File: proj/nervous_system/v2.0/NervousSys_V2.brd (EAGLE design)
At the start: 162.3 x 94.7 mm, 101 parts, among them IC2 PCA9615DP, IC3 PCA9615DP, IC4 PCA9615DP, IC5 PCA9615DP, IC6 PCA9615DP, IC7 PCA9615DP, IC8 PCA9615DP, IC9 PCA9615DP, J2 54602-908LF, J3 54602-908LF, J4 54602-908LF, J5 54602-908LF, J6 54602-908LF, J7 54602-908LF, J8 54602-908LF, J9 54602-908LF, T1 R-78E5.0-1.0, U1 TCA9548APWRPW24-M

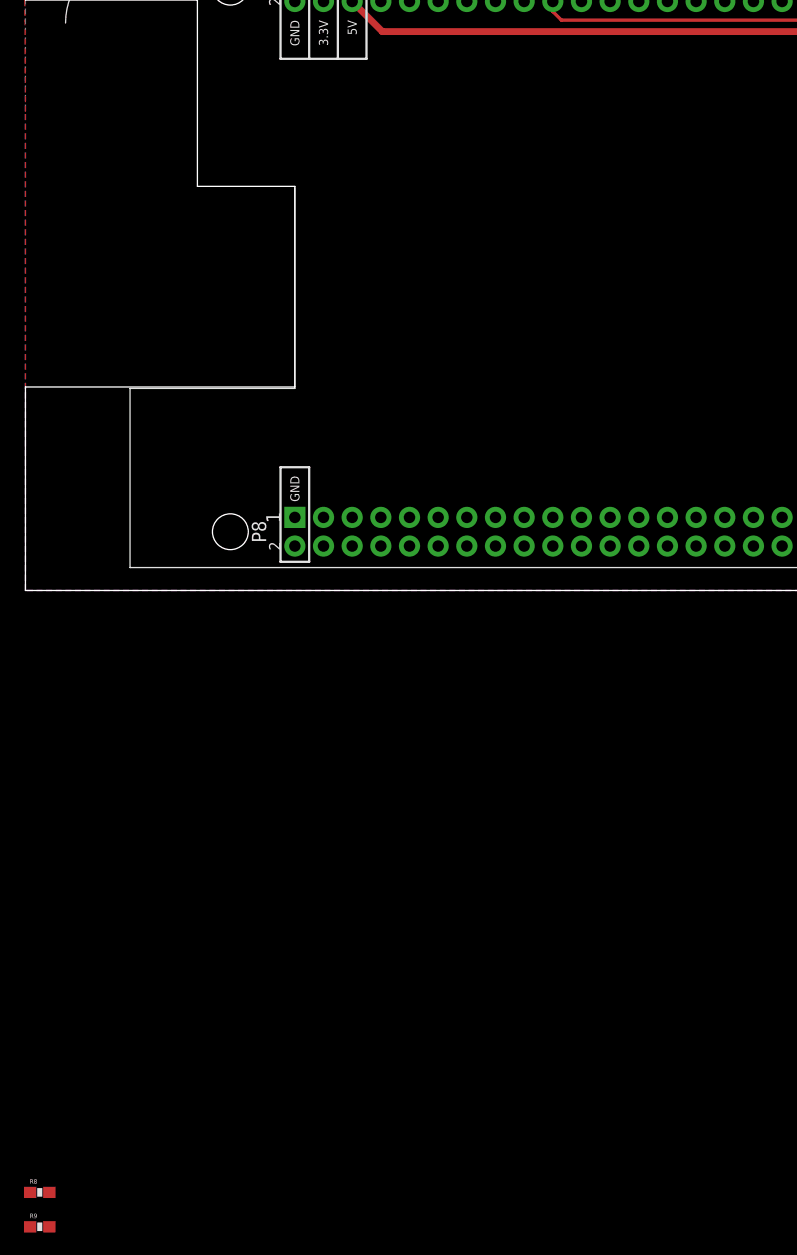
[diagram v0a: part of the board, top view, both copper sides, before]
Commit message: NS V2 Layout Change
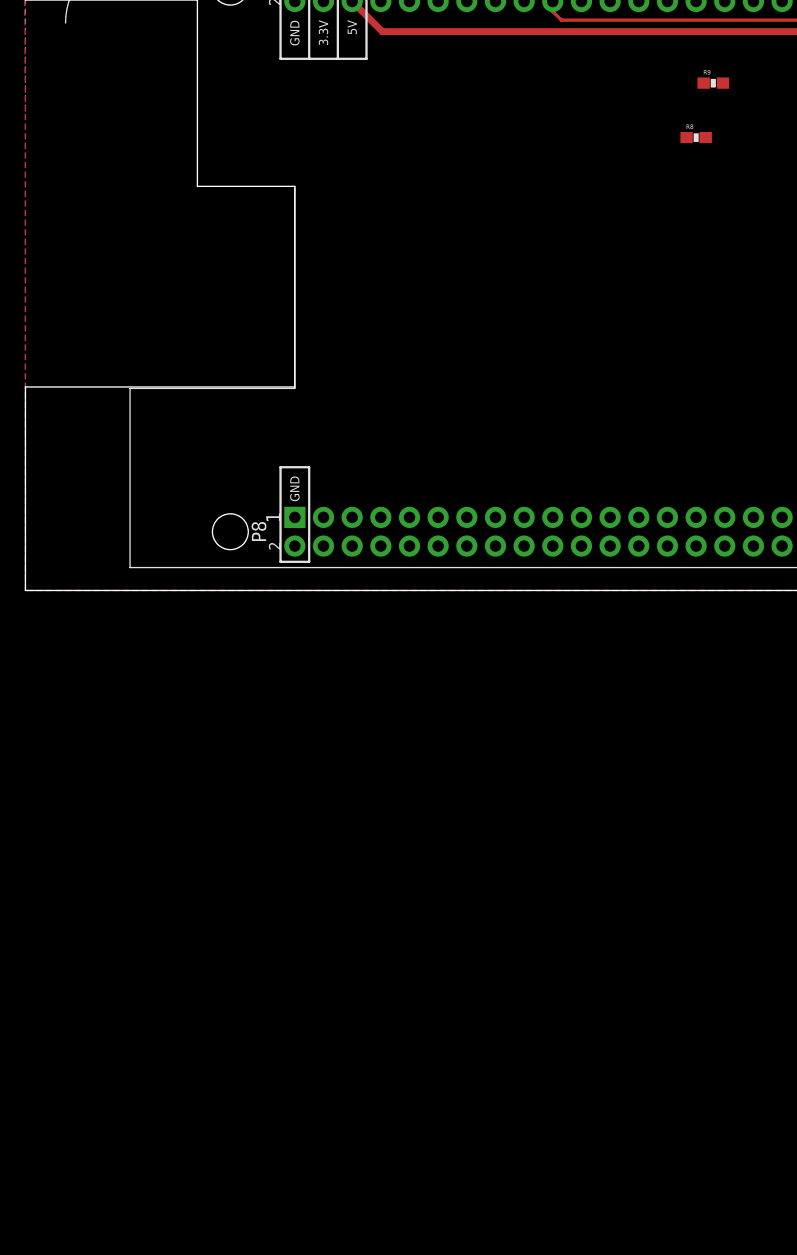
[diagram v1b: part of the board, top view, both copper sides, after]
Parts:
- moved R9 117.6 mm to (61.0, 45.0)
- moved R8 110.1 mm to (59.4, 40.1)
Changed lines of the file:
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@@
 </element>
 <element name="U$1" library="PJ-036ah" package="PJ-036AH" value="PJ-036AH" x="128.27" y="11.176" rot="R90"/>
-<element name="R8" library="SparkFun-Resistors" package="0603-RES" value="10K" x="1.27" y="-53.34">
-<attribute name="PROD_ID" value="RES-00824" x="1.27" y="-53.34" size="1.778" layer="27" display="off"/>
+<element name="R8" library="SparkFun-Resistors" package="0603-RES" value="10K" x="59.436" y="40.132">
+<attribute name="PROD_ID" value="RES-00824" x="59.436" y="40.132" size="1.778" layer="27" display="off"/>
 </element>
-<element name="R9" library="SparkFun-Resistors" package="0603-RES" value="10K" x="1.27" y="-56.388">
-<attribute name="PROD_ID" value="RES-00824" x="1.27" y="-56.388" size="1.778" layer="27" display="off"/>
+<element name="R9" library="SparkFun-Resistors" package="0603-RES" value="10K" x="60.96" y="44.958">
+<attribute name="PROD_ID" value="RES-00824" x="60.96" y="44.958" size="1.778" layer="27" display="off"/>
 </element>
 </elements>
@@
 <wire x1="82.55" y1="47.244" x2="79.248" y2="50.546" width="0.3048" layer="1"/>
 <contactref element="R9" pad="1"/>
-<wire x1="0.42" y1="-56.388" x2="47.498" y2="50.546" width="0" layer="19" extent="1-1"/>
+<wire x1="60.11" y1="44.958" x2="47.498" y2="50.546" width="0" layer="19" extent="1-1"/>
 </signal>
 <signal name="SCL">
@@
 <wire x1="57.91946875" y1="59.944" x2="47.752" y2="59.944" width="0.3048" layer="1"/>
 <contactref element="R8" pad="1"/>
-<wire x1="0.42" y1="-53.34" x2="46.736" y2="54.737" width="0" layer="19" extent="1-1"/>
+<wire x1="58.586" y1="40.132" x2="46.736" y2="54.737" width="0" layer="19" extent="1-1"/>
 </signal>
 <signal name="+3V3">
@@
 <contactref element="R9" pad="2"/>
 <wire x1="26.416" y1="54.737" x2="26.416" y2="52.197" width="0" layer="19" extent="1-1"/>
-<wire x1="2.12" y1="-53.34" x2="26.416" y2="52.197" width="0" layer="19" extent="1-1"/>
-<wire x1="2.12" y1="-56.388" x2="2.12" y2="-53.34" width="0" layer="19" extent="1-1"/>
+<wire x1="60.286" y1="40.132" x2="26.416" y2="52.197" width="0" layer="19" extent="1-1"/>
+<wire x1="61.81" y1="44.958" x2="60.286" y2="40.132" width="0" layer="19" extent="1-1"/>
 </signal>
 <signal name="RESET1">

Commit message: NSV2 Changes
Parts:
- moved R8 23.6 mm to (43.9, 57.9), turned to 180 degrees
- moved R9 16.9 mm to (44.2, 47.2), turned to 180 degrees
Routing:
- net +3V3: track 345.1 -> 383.7 mm
- net SDA: track 122.7 -> 132.7 mm, vias 0 -> 2
- net SCL: track 116.8 -> 118.7 mm
- net +5V: track 142.9 -> 144.4 mm
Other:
- board text added: "SCL Pullup"
- board text added: "SDA Pullup"
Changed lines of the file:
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@@
 <text x="7.112" y="56.896" size="1.778" layer="25">I2C
 CH:7</text>
+<text x="36.322" y="58.674" size="0.8128" layer="25">SCL Pullup</text>
+<text x="41.656" y="44.958" size="0.8128" layer="25">SDA Pullup</text>
 </plain>
 <attributes>
@@
 </element>
 <element name="U$1" library="PJ-036ah" package="PJ-036AH" value="PJ-036AH" x="128.27" y="11.176" rot="R90"/>
-<element name="R8" library="SparkFun-Resistors" package="0603-RES" value="10K" x="59.436" y="40.132">
-<attribute name="PROD_ID" value="RES-00824" x="59.436" y="40.132" size="1.778" layer="27" display="off"/>
-</element>
-<element name="R9" library="SparkFun-Resistors" package="0603-RES" value="10K" x="60.96" y="44.958">
-<attribute name="PROD_ID" value="RES-00824" x="60.96" y="44.958" size="1.778" layer="27" display="off"/>
+<element name="R8" library="SparkFun-Resistors" package="0603-RES" value="10K" x="43.942" y="57.912" rot="R180">
+<attribute name="PROD_ID" value="RES-00824" x="43.942" y="57.912" size="1.778" layer="27" rot="R180" display="off"/>
+</element>
+<element name="R9" library="SparkFun-Resistors" package="0603-RES" value="10K" x="44.196" y="47.244" rot="R180">
+<attribute name="PROD_ID" value="RES-00824" x="44.196" y="47.244" size="1.778" layer="27" rot="R180" display="off"/>
 </element>
 </elements>
@@
 <vertex x="154.686" y="73.66"/>
 <vertex x="1.016" y="73.66"/>
-<vertex x="1.016" y="94.742"/>
-<vertex x="161.798" y="94.742"/>
+<vertex x="1.524" y="95.25"/>
+<vertex x="162.306" y="95.25"/>
 <vertex x="161.798" y="33.528"/>
 </polygon>
@@
 <wire x1="87.376" y1="48.768" x2="85.852" y2="47.244" width="0.3048" layer="1"/>
 <wire x1="85.852" y1="47.244" x2="82.55" y2="47.244" width="0.3048" layer="1"/>
-<wire x1="79.248" y1="50.546" x2="47.498" y2="50.546" width="0.3048" layer="1"/>
+<wire x1="79.248" y1="50.546" x2="49.53" y2="50.546" width="0.3048" layer="1"/>
+<wire x1="49.53" y1="50.546" x2="47.498" y2="50.546" width="0.3048" layer="1"/>
 <wire x1="47.498" y1="50.546" x2="46.736" y2="51.308" width="0.3048" layer="1"/>
 <wire x1="46.736" y1="51.308" x2="46.736" y2="52.197" width="0.3048" layer="1"/>
 <wire x1="82.55" y1="47.244" x2="79.248" y2="50.546" width="0.3048" layer="1"/>
 <contactref element="R9" pad="1"/>
-<wire x1="60.11" y1="44.958" x2="47.498" y2="50.546" width="0" layer="19" extent="1-1"/>
+<wire x1="45.046" y1="47.244" x2="46.57" y2="45.72" width="0.3048" layer="1"/>
+<wire x1="46.57" y1="45.72" x2="49.53" y2="45.72" width="0.3048" layer="1"/>
+<via x="49.53" y="45.72" extent="1-16" drill="0.35"/>
+<wire x1="49.53" y1="45.72" x2="49.53" y2="49.276" width="0.3048" layer="16"/>
+<via x="49.53" y="49.276" extent="1-16" drill="0.35"/>
+<wire x1="49.53" y1="49.276" x2="49.53" y2="50.546" width="0.3048" layer="1"/>
 </signal>
 <signal name="SCL">
@@
 <wire x1="77.0479125" y1="58.90334375" x2="58.960125" y2="58.90334375" width="0.3048" layer="1"/>
 <wire x1="47.752" y1="59.944" x2="46.736" y2="58.928" width="0.3048" layer="1"/>
-<wire x1="46.736" y1="58.928" x2="46.736" y2="54.737" width="0.3048" layer="1"/>
+<wire x1="46.736" y1="58.928" x2="46.736" y2="57.912" width="0.3048" layer="1"/>
+<wire x1="46.736" y1="57.912" x2="46.736" y2="54.737" width="0.3048" layer="1"/>
 <wire x1="57.91946875" y1="59.944" x2="47.752" y2="59.944" width="0.3048" layer="1"/>
 <contactref element="R8" pad="1"/>
-<wire x1="58.586" y1="40.132" x2="46.736" y2="54.737" width="0" layer="19" extent="1-1"/>
+<wire x1="44.792" y1="57.912" x2="46.736" y2="57.912" width="0.3048" layer="1"/>
 </signal>
 <signal name="+3V3">
@@
 <contactref element="R8" pad="2"/>
 <contactref element="R9" pad="2"/>
+<wire x1="43.346" y1="47.244" x2="42.076" y2="48.514" width="0.3048" layer="1"/>
+<wire x1="42.076" y1="48.514" x2="27.686" y2="48.514" width="0.3048" layer="1"/>
+<wire x1="27.686" y1="48.514" x2="26.162" y2="50.038" width="0.3048" layer="1"/>
+<wire x1="26.162" y1="50.038" x2="26.162" y2="51.943" width="0.3048" layer="1"/>
+<wire x1="26.162" y1="51.943" x2="26.416" y2="52.197" width="0.3048" layer="1"/>
+<wire x1="43.092" y1="57.912" x2="29.591" y2="57.912" width="0.3048" layer="1"/>
+<wire x1="29.591" y1="57.912" x2="26.416" y2="54.737" width="0.3048" layer="1"/>
 <wire x1="26.416" y1="54.737" x2="26.416" y2="52.197" width="0" layer="19" extent="1-1"/>
-<wire x1="60.286" y1="40.132" x2="26.416" y2="52.197" width="0" layer="19" extent="1-1"/>
-<wire x1="61.81" y1="44.958" x2="60.286" y2="40.132" width="0" layer="19" extent="1-1"/>
 </signal>
 <signal name="RESET1">
@@
 <wire x1="86.16763125" y1="46.482" x2="88.138" y2="48.45236875" width="0.6096" layer="1"/>
 <wire x1="88.138" y1="48.45236875" x2="88.138" y2="55.31036875" width="0.6096" layer="1"/>
-<wire x1="31.623" y1="49.53" x2="79.18636875" y2="49.53" width="0.6096" layer="1"/>
+<wire x1="31.623" y1="49.53" x2="46.736" y2="49.53" width="0.6096" layer="1"/>
+<wire x1="46.736" y1="49.53" x2="48.514" y2="47.752" width="0.6096" layer="1"/>
+<wire x1="48.514" y1="47.752" x2="51.054" y2="47.752" width="0.6096" layer="1"/>
+<wire x1="51.054" y1="47.752" x2="52.832" y2="49.53" width="0.6096" layer="1"/>
+<wire x1="52.832" y1="49.53" x2="79.18636875" y2="49.53" width="0.6096" layer="1"/>
 <wire x1="88.930815625" y1="56.103184375" x2="96.096228125" y2="56.103184375" width="0.6096" layer="1"/>
 <wire x1="120.5484" y1="53.7972" x2="122.7836" y2="51.562" width="0.6096" layer="1"/>

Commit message: NSV2
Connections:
- net +3V3: no longer IC2.10, IC3.10, IC4.10, IC5.10, IC6.10, IC7.10, IC8.10, IC9.10, R18.1, R19.2, R26.1, R27.2, R34.1, R35.2, R42.1, R43.2, R50.1, R51.2, R58.1, R59.2, R66.1, R67.2, R74.1, R75.2
- net +5V: now also IC2.10, IC3.10, IC4.10, IC5.10, IC6.10, IC7.10, IC8.10, IC9.10, R18.1, R19.2, R26.1, R27.2, R34.1, R35.2, R42.1, R43.2, R50.1, R51.2, R58.1, R59.2, R66.1, R67.2, R74.1, R75.2
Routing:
- net +5V: track 144.4 -> 363.8 mm, vias 0 -> 9
- net +3V3: track 383.7 -> 304.4 mm

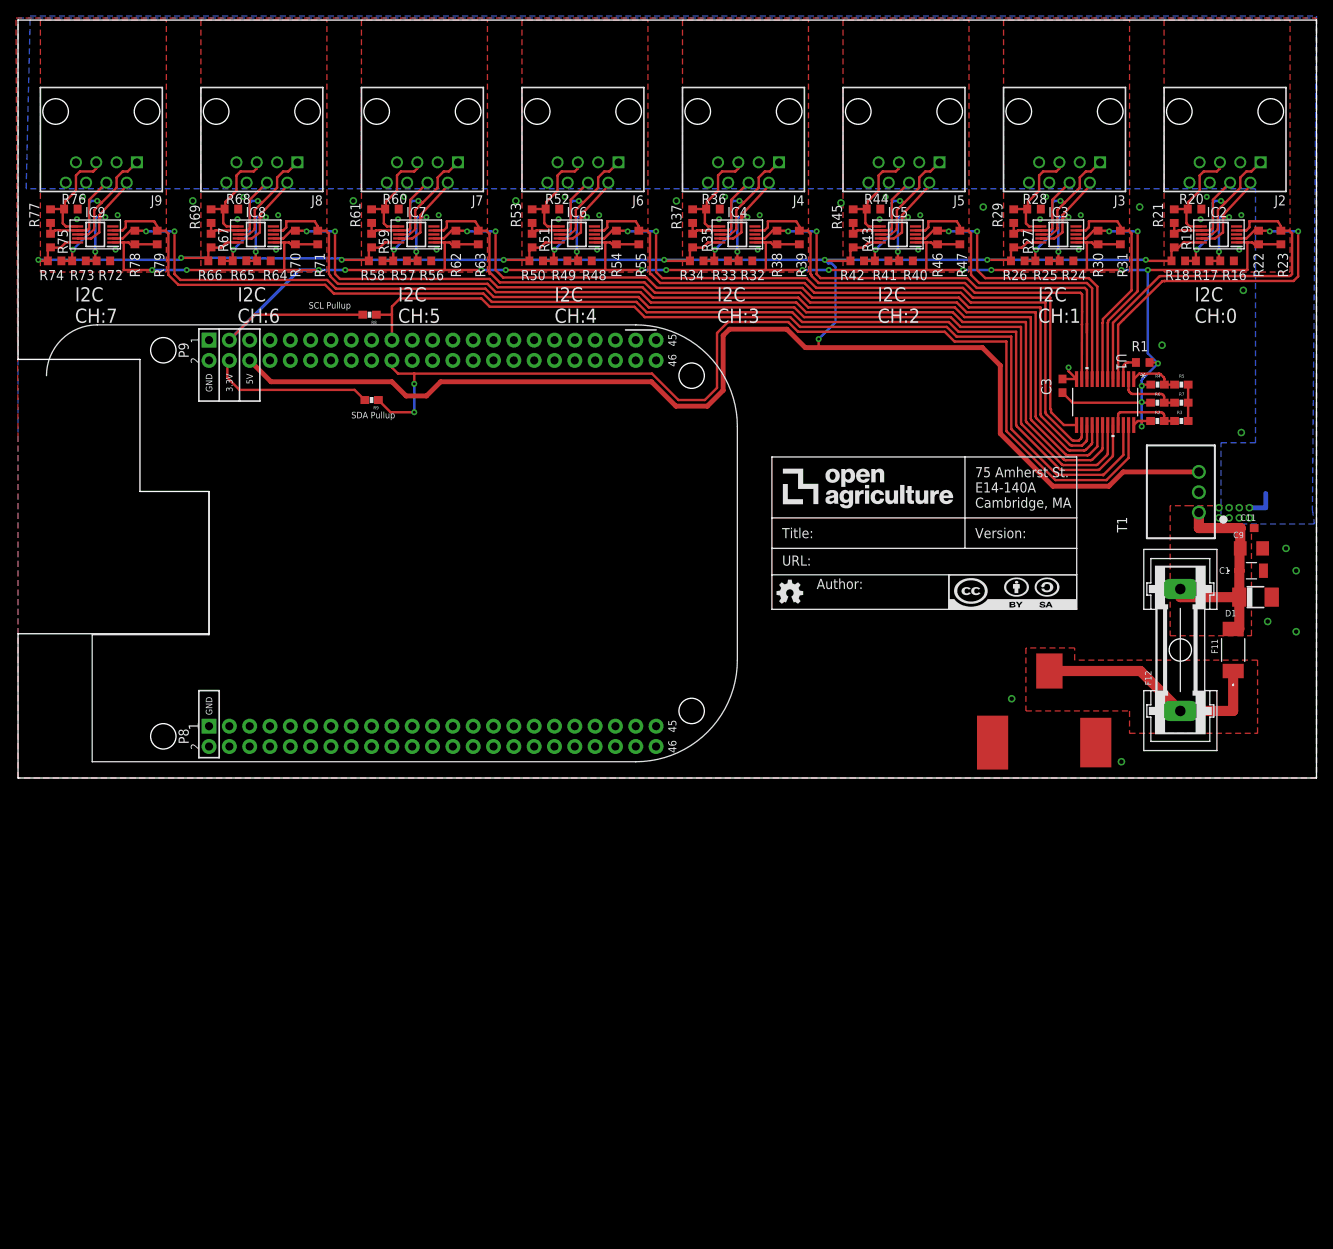
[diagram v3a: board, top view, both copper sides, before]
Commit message: NSV2.0 Brd Update
Photon header, indicator leds etc
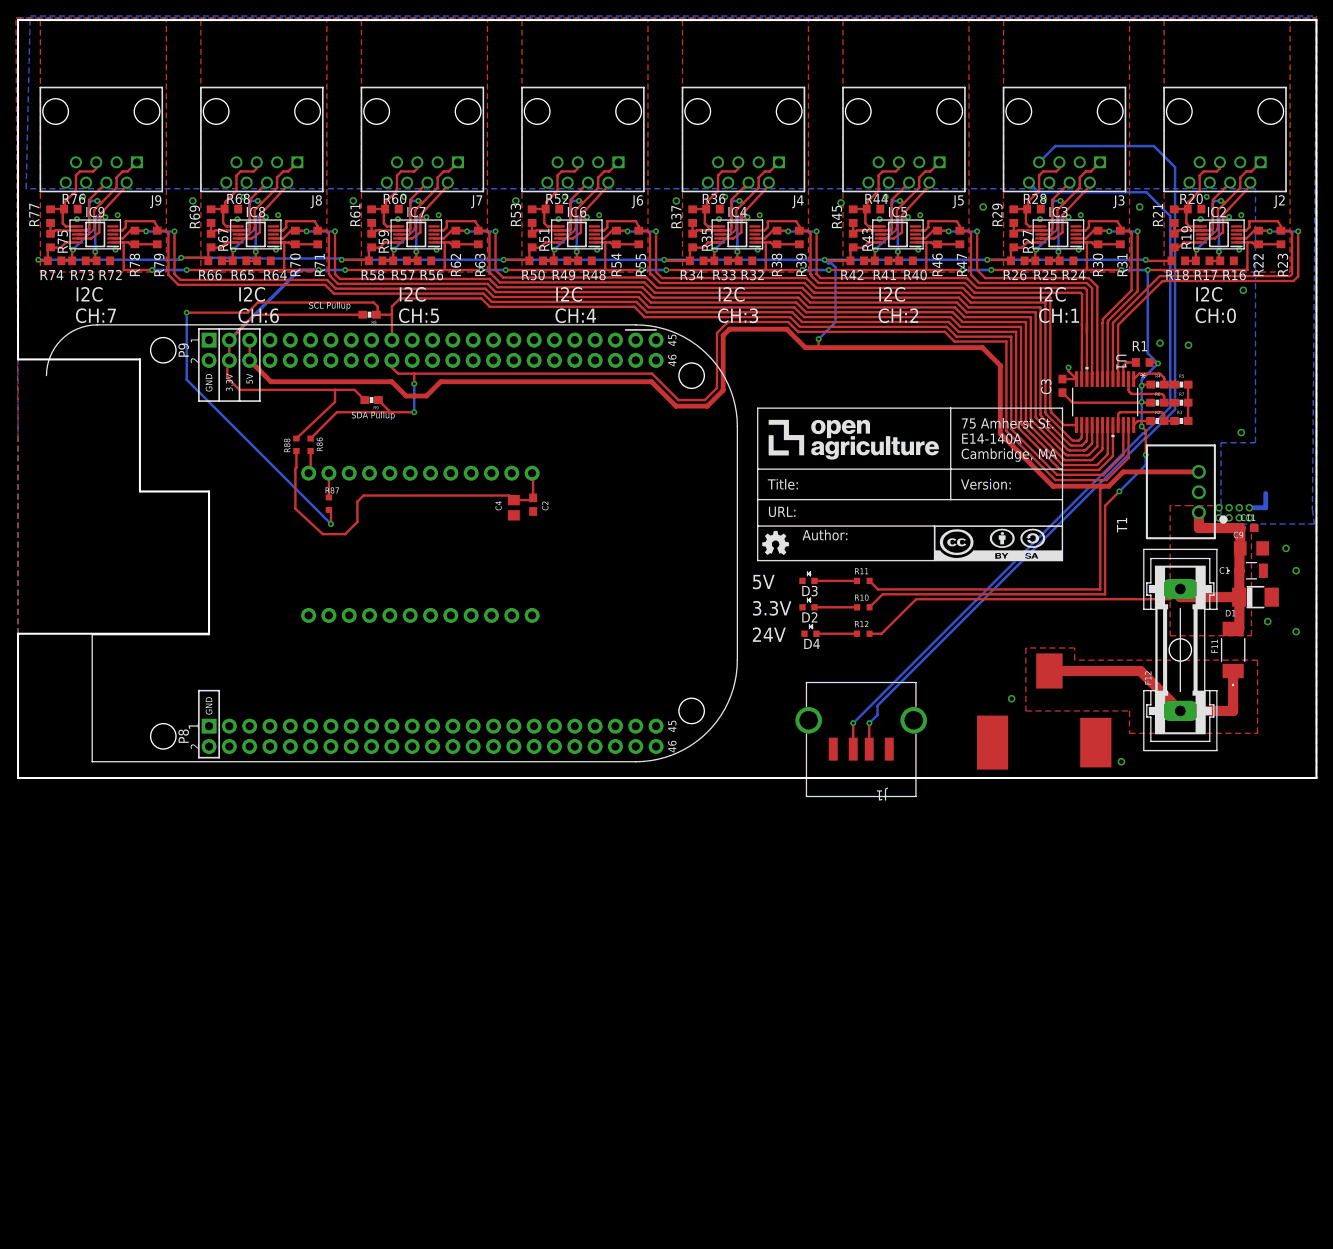
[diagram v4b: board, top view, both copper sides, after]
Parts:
- added C2: 0.1uF, openag-capacitors:C0603
- added C4: 4.7uF, openag-capacitors:C0805
- added D2, D3, D4: APT1608CGCK, openag-diodes:CHIPLED_0603
- added J1: 87583-2010BLF, openag-connectors:CONN_USB-87583
- added R10, R11, R12: 100 OHM, openag-resistors:RC0603N
- added R86, R87, R88: 0 OHM, openag-resistors:RC0603N
- added U2: PHOTONH, openag-microcontrollers:PHOTON
- moved ATTRIBUTES 6.35 mm to (92.5, 27.2)
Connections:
- new net N$12: D2.A, R10.1
- new net N$2: D3.A, R11.1
- new net N$4: D4.A, R12.1
- new net N$9: C2.1, C4.1, R88.1, U2.24
- new net PHOTON_A0: U2.12
- new net PHOTON_A1: U2.11
- new net PHOTON_D2: U2.15
- new net PHOTON_D3: U2.16
- new net PHOTON_D4: U2.17
- new net PHOTON_RX: U2.4
- new net PHOTON_SCL: R87.1, U2.14
- new net PHOTON_SDA: R86.1, U2.13
- new net PHOTON_TX: U2.3
- new net VBAT: U2.22
- new net VIN: U2.1
- net +24V: now also R12.2
- net +3V3: now also R10.2, R88.2
- net +5V: now also R11.2
- net GND: now also C2.2, C4.2, D2.C, D3.C, D4.C, J1.1, U2.2, U2.21
- net SCL: now also R87.2
- net SDA: now also R86.2
- net USBM1: now also J1.3
- net USBP1: now also J1.2
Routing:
- net USBP1: track 0.00 -> 107.6 mm, vias 0 -> 1
- net USBM1: track 0.00 -> 102.5 mm, vias 0 -> 1
- net +3V3: track 304.4 -> 368.5 mm, vias 18 -> 20
- net SCL: track 118.7 -> 180.1 mm, vias 0 -> 2
- net N$9: track 0.00 -> 45.2 mm
- net +5V: track 363.8 -> 408.6 mm
- net +24V: track 32.9 -> 74.1 mm
- net SDA: track 132.7 -> 144.0 mm
- net N$2: track 0.00 -> 5.33 mm
- net N$12: track 0.00 -> 5.33 mm
- net N$4: track 0.00 -> 5.08 mm
- net PHOTON_SCL: track 0.00 -> 3.03 mm
- net PHOTON_SDA: track 0.00 -> 2.88 mm
- net GND: vias 49 -> 50
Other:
- board text added: "24V"
